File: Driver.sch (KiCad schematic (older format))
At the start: 10 parts

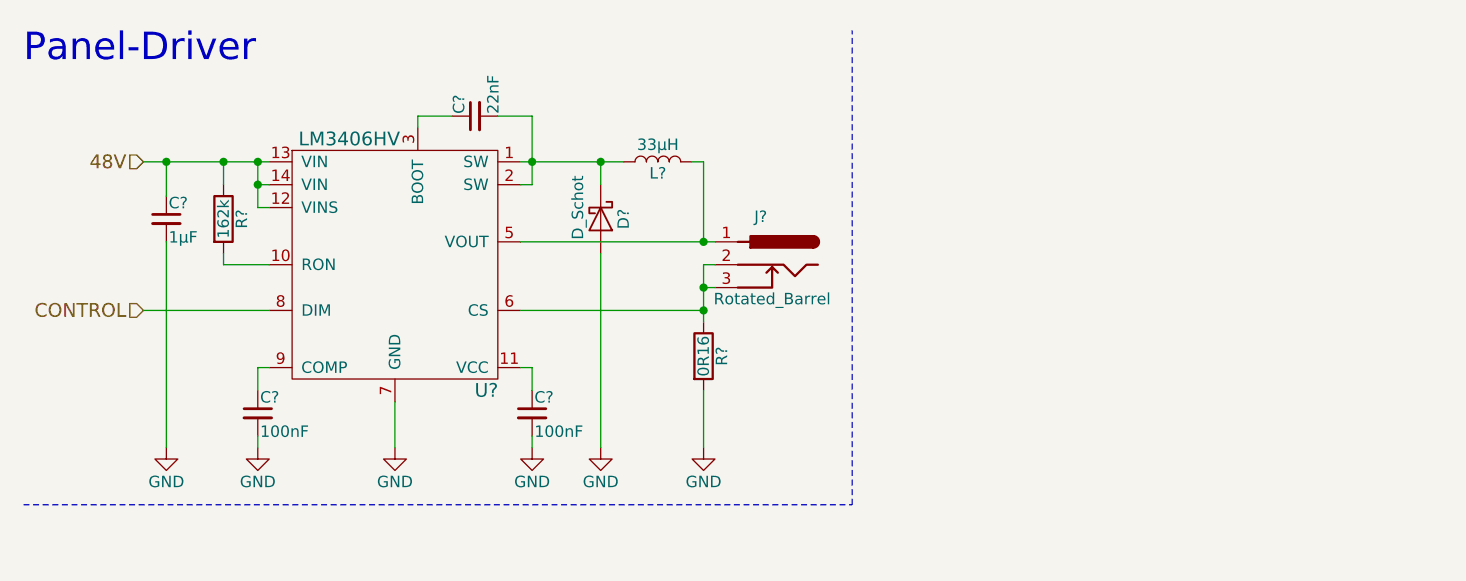
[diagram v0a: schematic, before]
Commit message: Merged RGB- and Panel-Drivers into a single Sheet
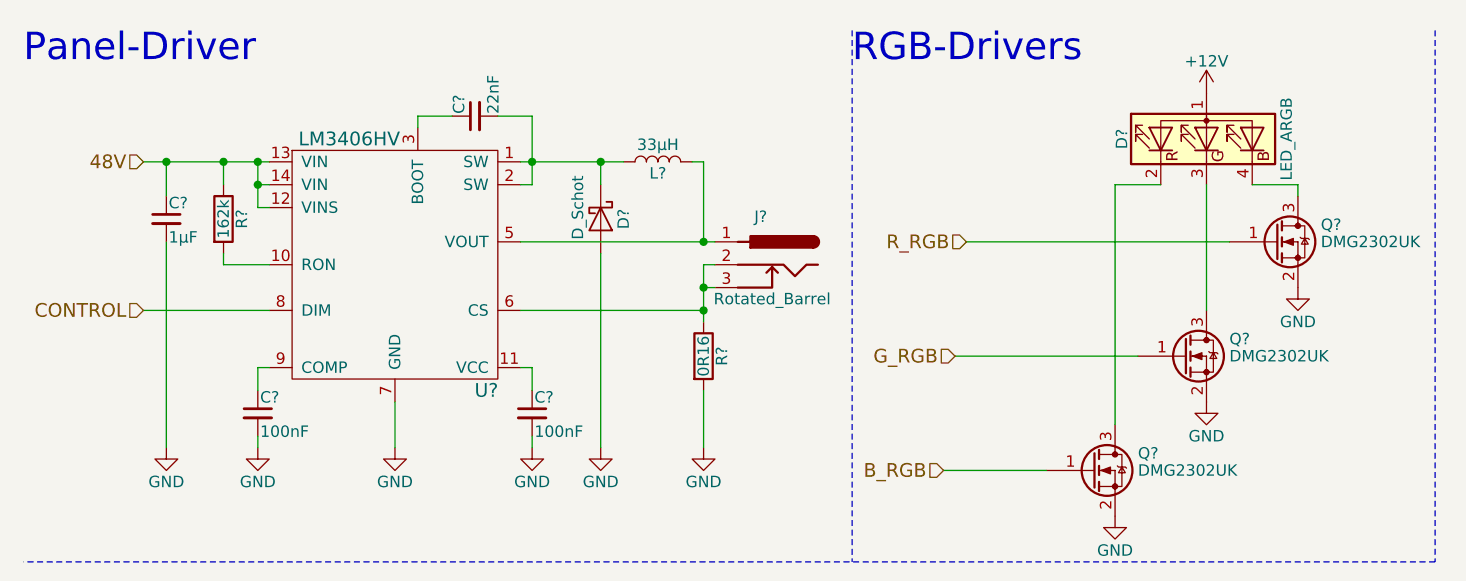
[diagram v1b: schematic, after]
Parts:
- added D?: LED_ARGB, symbol LED_ARGB
- added Q? (x3): DMG2302UK, TO_SOT_Packages_SMD:SOT-23, symbol 2N7002
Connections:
- net GND: now also Q?.2 (S), Q?.2 (S), Q?.2 (S)
- new net: D?.2 (RK), Q?.3 (D)
- new net: D?.3 (GK), Q?.3 (D)
- new net: D?.4 (BK), Q?.3 (D)
- new net +12V: D?.1 (A)
- new net B_RGB: Q?.1 (G)
- new net G_RGB: Q?.1 (G)
- new net R_RGB: Q?.1 (G)
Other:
- note added: "RGB-Drivers"
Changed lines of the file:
@@
 $Descr A4 11693 8268
 encoding utf-8
-Sheet 4 5
+Sheet 3 5
 Title ""
 Date ""
@@
 AR Path="/5A4C3F5F/5A777BDD" Ref="#PWR043"  Part="1"
 AR Path="/5A4C34AF/5A777BDD" Ref="#PWR038"  Part="1"
-F 0 "#PWR043" H 1500 2050 50  0001 C CNN
+F 0 "#PWR038" H 1500 2050 50  0001 C CNN
 F 1 "GND" H 1500 2150 50  0000 C CNN
 F 2 "" H 1500 2300 50  0001 C CNN
@@
 AR Path="/5A4C3F5F/5A777CDA" Ref="#PWR044"  Part="1"
 AR Path="/5A4C34AF/5A777CDA" Ref="#PWR039"  Part="1"
-F 0 "#PWR044" H 2700 2050 50  0001 C CNN
+F 0 "#PWR039" H 2700 2050 50  0001 C CNN
 F 1 "GND" H 2700 2150 50  0000 C CNN
 F 2 "" H 2700 2300 50  0001 C CNN
@@
 AR Path="/5A4C3F5F/5A777FA3" Ref="#PWR045"  Part="1"
 AR Path="/5A4C34AF/5A777FA3" Ref="#PWR040"  Part="1"
-F 0 "#PWR045" H 2100 2050 50  0001 C CNN
+F 0 "#PWR040" H 2100 2050 50  0001 C CNN
 F 1 "GND" H 2100 2150 50  0000 C CNN
 F 2 "" H 2100 2300 50  0001 C CNN
@@
 AR Path="/5A4C3F5F/5A778B62" Ref="#PWR046"  Part="1"
 AR Path="/5A4C34AF/5A778B62" Ref="#PWR041"  Part="1"
-F 0 "#PWR046" H 3000 2050 50  0001 C CNN
+F 0 "#PWR041" H 3000 2050 50  0001 C CNN
 F 1 "GND" H 3000 2150 50  0000 C CNN
 F 2 "" H 3000 2300 50  0001 C CNN
@@
 AR Path="/5A4C34AF/5A77A9CB" Ref="#PWR042"  Part="1"
 AR Path="/5A4C3F5F/5A77A9CB" Ref="#PWR047"  Part="1"
-F 0 "#PWR047" H 3450 2050 50  0001 C CNN
+F 0 "#PWR042" H 3450 2050 50  0001 C CNN
 F 1 "GND" H 3450 2150 50  0000 C CNN
 F 2 "" H 3450 2300 50  0001 C CNN
@@
 Text Notes 475  625  0    120  ~ 0
 Panel-Driver
+Text HLabel 4600 1400 0    60   Input ~ 0
+R_RGB
+Text HLabel 4500 2400 0    60   Input ~ 0
+B_RGB
+Text HLabel 4550 1900 0    60   Input ~ 0
+G_RGB
+$Comp
+L LED_ARGB D?
+U 1 1 5A83A3D8
+P 5650 950
+F 0 "D?" H 5650 1320 50  0000 C CNN
+F 1 "LED_ARGB" H 5650 600 50  0000 C CNN
+F 2 "" H 5650 900 50  0001 C CNN
+F 3 "" H 5650 900 50  0001 C CNN
+	1    5650 950
+	0    -1   -1   0
+$EndComp
+$Comp
+L +12V #PWR?
+U 1 1 5A83A3DF
+P 5650 750
+F 0 "#PWR?" H 5650 600 50  0001 C CNN
+F 1 "+12V" H 5650 890 50  0000 C CNN
+F 2 "" H 5650 750 50  0001 C CNN
+F 3 "" H 5650 750 50  0001 C CNN
+	1    5650 750
+	1    0    0    -1
+$EndComp
+Wire Wire Line
+	5250 1150 5450 1150
+Wire Wire Line
+	4600 1400 5750 1400
+Wire Wire Line
+	4550 1900 5350 1900
+Wire Wire Line
+	4500 2400 4950 2400
+$Comp
+L GND #PWR?
+U 1 1 5A83A3E9
+P 6050 1600
+F 0 "#PWR?" H 6050 1350 50  0001 C CNN
+F 1 "GND" H 6050 1450 50  0000 C CNN
+F 2 "" H 6050 1600 50  0001 C CNN
+F 3 "" H 6050 1600 50  0001 C CNN
+	1    6050 1600
+	1    0    0    -1
+$EndComp
+$Comp
+L GND #PWR?
+U 1 1 5A83A3EF
+P 5650 2100
+F 0 "#PWR?" H 5650 1850 50  0001 C CNN
+F 1 "GND" H 5650 1950 50  0000 C CNN
+F 2 "" H 5650 2100 50  0001 C CNN
+F 3 "" H 5650 2100 50  0001 C CNN
+	1    5650 2100
+	1    0    0    -1
+$EndComp
+$Comp
+L GND #PWR?
+U 1 1 5A83A3F5
+P 5250 2600
+F 0 "#PWR?" H 5250 2350 50  0001 C CNN
+F 1 "GND" H 5250 2450 50  0000 C CNN
+F 2 "" H 5250 2600 50  0001 C CNN
+F 3 "" H 5250 2600 50  0001 C CNN
+	1    5250 2600
+	1    0    0    -1
+$EndComp
+Wire Wire Line
+	5250 1150 5250 2200
+Wire Wire Line
+	5650 1150 5650 1700
+$Comp
+L 2N7002 Q?
+U 1 1 5A83A3FE
+P 5150 2400
+F 0 "Q?" H 5350 2475 50  0000 L CNN
+F 1 "DMG2302UK" H 5350 2400 50  0000 L CNN
+F 2 "TO_SOT_Packages_SMD:SOT-23" H 5350 2325 50  0001 L CIN
+F 3 "https://www.diodes.com/assets/Datasheets/DMG2302UK.pdf" H 5150 2400 50  0001 L CNN
+F 4 "https://www.digikey.com/product-detail/en/diodes-incorporated/DMG2302UK-7/DMG2302UK-7DICT-ND/6010163" H 5150 2400 60  0001 C CNN "Digikey"
+	1    5150 2400
+	1    0    0    -1
+$EndComp
+$Comp
+L 2N7002 Q?
+U 1 1 5A83A406
+P 5550 1900
+F 0 "Q?" H 5750 1975 50  0000 L CNN
+F 1 "DMG2302UK" H 5750 1900 50  0000 L CNN
+F 2 "TO_SOT_Packages_SMD:SOT-23" H 5750 1825 50  0001 L CIN
+F 3 "https://www.diodes.com/assets/Datasheets/DMG2302UK.pdf" H 5550 1900 50  0001 L CNN
+F 4 "https://www.digikey.com/product-detail/en/diodes-incorporated/DMG2302UK-7/DMG2302UK-7DICT-ND/6010163" H 5550 1900 60  0001 C CNN "Digikey"
+	1    5550 1900
+	1    0    0    -1
+$EndComp
+$Comp
+L 2N7002 Q?
+U 1 1 5A83A40E
+P 5950 1400
+F 0 "Q?" H 6150 1475 50  0000 L CNN
+F 1 "DMG2302UK" H 6150 1400 50  0000 L CNN
+F 2 "TO_SOT_Packages_SMD:SOT-23" H 6150 1325 50  0001 L CIN
+F 3 "https://www.diodes.com/assets/Datasheets/DMG2302UK.pdf" H 5950 1400 50  0001 L CNN
+F 4 "https://www.digikey.com/product-detail/en/diodes-incorporated/DMG2302UK-7/DMG2302UK-7DICT-ND/6010163" H 5950 1400 60  0001 C CNN "Digikey"
+	1    5950 1400
+	1    0    0    -1
+$EndComp
+Wire Wire Line
+	6050 1200 6050 1150
+Wire Wire Line
+	6050 1150 5850 1150
+Text Notes 4100 625  0    120  ~ 0
+RGB-Drivers
 Wire Notes Line
-	475  2550 4100 2550
+	6650 2800 475  2800
 Wire Notes Line
-	4100 2550 4100 475
+	6650 475  6650 2800
+Wire Notes Line
+	4100 475  4100 2800
 $EndSCHEMATC

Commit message: Moved the transceivers into their own sheet
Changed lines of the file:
@@
 $Descr A4 11693 8268
 encoding utf-8
-Sheet 3 5
+Sheet 4 7
 Title ""
 Date ""
@@
 AR Path="/5A4C3F5F/5A777BDD" Ref="#PWR043"  Part="1"
 AR Path="/5A4C34AF/5A777BDD" Ref="#PWR038"  Part="1"
-F 0 "#PWR038" H 1500 2050 50  0001 C CNN
+F 0 "#PWR043" H 1500 2050 50  0001 C CNN
 F 1 "GND" H 1500 2150 50  0000 C CNN
 F 2 "" H 1500 2300 50  0001 C CNN
@@
 AR Path="/5A4C3F5F/5A777CDA" Ref="#PWR044"  Part="1"
 AR Path="/5A4C34AF/5A777CDA" Ref="#PWR039"  Part="1"
-F 0 "#PWR039" H 2700 2050 50  0001 C CNN
+F 0 "#PWR044" H 2700 2050 50  0001 C CNN
 F 1 "GND" H 2700 2150 50  0000 C CNN
 F 2 "" H 2700 2300 50  0001 C CNN
@@
 AR Path="/5A4C3F5F/5A777FA3" Ref="#PWR045"  Part="1"
 AR Path="/5A4C34AF/5A777FA3" Ref="#PWR040"  Part="1"
-F 0 "#PWR040" H 2100 2050 50  0001 C CNN
+F 0 "#PWR045" H 2100 2050 50  0001 C CNN
 F 1 "GND" H 2100 2150 50  0000 C CNN
 F 2 "" H 2100 2300 50  0001 C CNN
@@
 	1500 1250 1550 1250
 Wire Wire Line
-	1500 1050 1500 1150
-Wire Wire Line
-	1500 1150 1500 1250
+	1500 1050 1500 1250
 Wire Wire Line
 	1500 1150 1550 1150
 Connection ~ 1500 1150
 Wire Wire Line
-	1000 1050 1100 1050
-Wire Wire Line
-	1100 1050 1350 1050
-Wire Wire Line
-	1350 1050 1500 1050
-Wire Wire Line
-	1500 1050 1550 1050
+	1000 1050 1550 1050
 Connection ~ 1500 1050
 Wire Wire Line
@@
 	2550 850  2700 850
 Wire Wire Line
-	2650 1050 2700 1050
-Wire Wire Line
-	2700 1050 3000 1050
-Wire Wire Line
-	3000 1050 3100 1050
-Wire Wire Line
-	2700 850  2700 1050
-Wire Wire Line
-	2700 1050 2700 1150
+	2650 1050 3100 1050
+Wire Wire Line
+	2700 850  2700 1150
 Wire Wire Line
 	1350 1500 1350 1450
@@
 AR Path="/5A4C3F5F/5A778B62" Ref="#PWR046"  Part="1"
 AR Path="/5A4C34AF/5A778B62" Ref="#PWR041"  Part="1"
-F 0 "#PWR041" H 3000 2050 50  0001 C CNN
+F 0 "#PWR046" H 3000 2050 50  0001 C CNN
 F 1 "GND" H 3000 2150 50  0000 C CNN
 F 2 "" H 3000 2300 50  0001 C CNN
@@
 	3450 1050 3450 1400
 Wire Wire Line
-	2650 1400 3450 1400
-Wire Wire Line
-	3450 1400 3500 1400
+	2650 1400 3500 1400
 Connection ~ 3450 1400
 $Comp
@@
 $EndComp
 Wire Wire Line
-	3450 1500 3450 1600
-Wire Wire Line
-	3450 1600 3450 1700
-Wire Wire Line
-	3450 1700 3450 1750
+	3450 1500 3450 1750
 Wire Wire Line
 	3450 1500 3500 1500
@@
 AR Path="/5A4C34AF/5A77A9CB" Ref="#PWR042"  Part="1"
 AR Path="/5A4C3F5F/5A77A9CB" Ref="#PWR047"  Part="1"
-F 0 "#PWR042" H 3450 2050 50  0001 C CNN
+F 0 "#PWR047" H 3450 2050 50  0001 C CNN
 F 1 "GND" H 3450 2150 50  0000 C CNN
 F 2 "" H 3450 2300 50  0001 C CNN

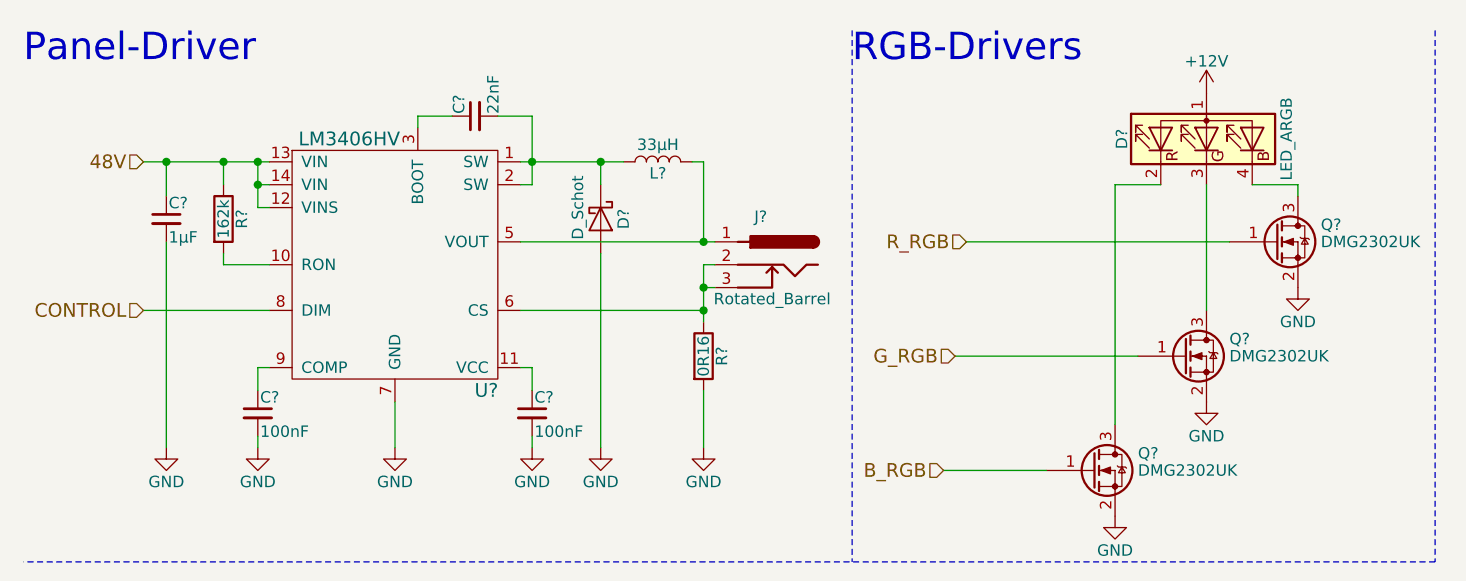
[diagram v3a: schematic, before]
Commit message: Added Gate-Resistors
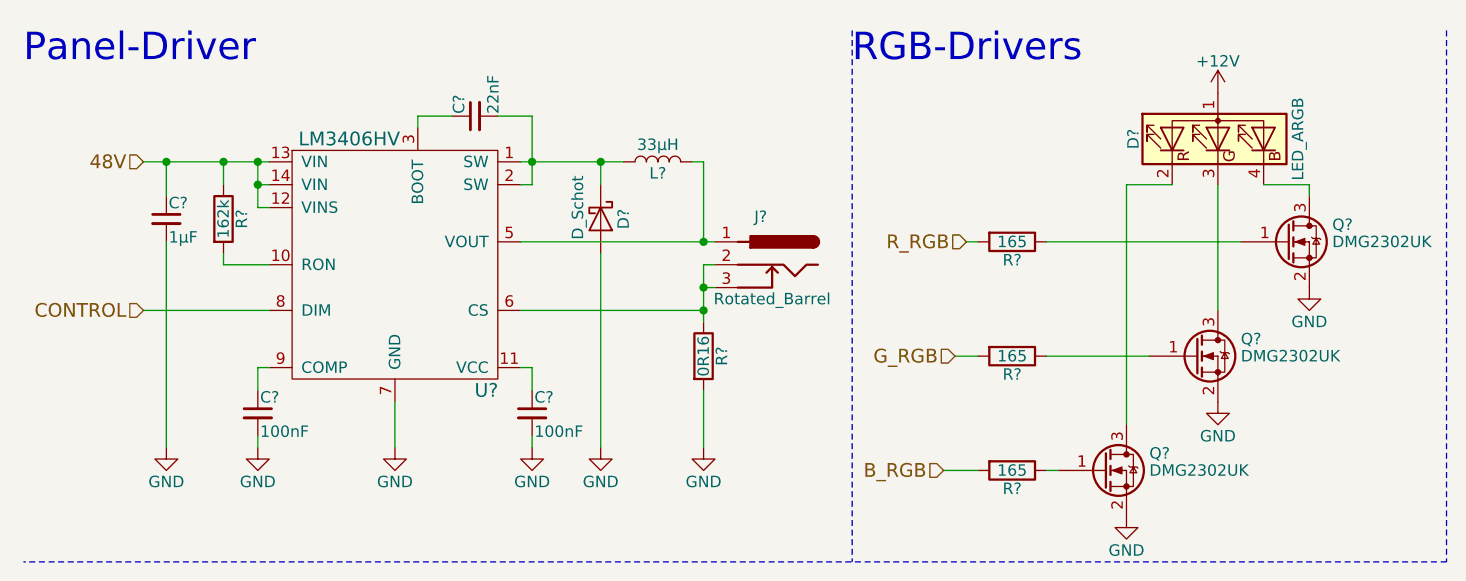
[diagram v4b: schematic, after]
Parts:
- added R? (x3): 165, symbol R
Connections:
- net B_RGB: now also R?.2; no longer Q?.1 (G)
- net G_RGB: now also R?.2; no longer Q?.1 (G)
- net R_RGB: now also R?.2; no longer Q?.1 (G)
- new net: Q?.1 (G), R?.1 (x3)
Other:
- moved on the sheet: D?, Q?
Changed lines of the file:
@@
 L LED_ARGB D?
 U 1 1 5A83A3D8
-P 5650 950
+P 5700 950
 AR Path="/5A4C3F5F/5A83A3D8" Ref="D?"  Part="1"
 AR Path="/5A4C442B/5A83A3D8" Ref="D?"  Part="1"
-F 0 "D?" H 5650 1320 50  0000 C CNN
-F 1 "LED_ARGB" H 5650 600 50  0000 C CNN
-F 2 "" H 5650 900 50  0001 C CNN
-F 3 "" H 5650 900 50  0001 C CNN
-	1    5650 950
+F 0 "D?" H 5700 1320 50  0000 C CNN
+F 1 "LED_ARGB" H 5700 600 50  0000 C CNN
+F 2 "" H 5700 900 50  0001 C CNN
+F 3 "" H 5700 900 50  0001 C CNN
+	1    5700 950
 	0    -1   -1   0
 $EndComp
@@
 L +12V #PWR?
 U 1 1 5A83A3DF
-P 5650 750
+P 5700 750
 AR Path="/5A4C3F5F/5A83A3DF" Ref="#PWR?"  Part="1"
 AR Path="/5A4C442B/5A83A3DF" Ref="#PWR?"  Part="1"
-F 0 "#PWR?" H 5650 600 50  0001 C CNN
-F 1 "+12V" H 5650 890 50  0000 C CNN
-F 2 "" H 5650 750 50  0001 C CNN
-F 3 "" H 5650 750 50  0001 C CNN
-	1    5650 750
+F 0 "#PWR?" H 5700 600 50  0001 C CNN
+F 1 "+12V" H 5700 890 50  0000 C CNN
+F 2 "" H 5700 750 50  0001 C CNN
+F 3 "" H 5700 750 50  0001 C CNN
+	1    5700 750
 	1    0    0    -1
 $EndComp
 Wire Wire Line
-	5250 1150 5450 1150
+	5300 1150 5500 1150
 Wire Wire Line
-	4600 1400 5750 1400
-Wire Wire Line
-	4550 1900 5350 1900
-Wire Wire Line
-	4500 2400 4950 2400
+	4950 1900 5400 1900
 $Comp
 L GND #PWR?
 U 1 1 5A83A3E9
-P 6050 1600
+P 6100 1600
 AR Path="/5A4C3F5F/5A83A3E9" Ref="#PWR?"  Part="1"
 AR Path="/5A4C442B/5A83A3E9" Ref="#PWR?"  Part="1"
-F 0 "#PWR?" H 6050 1350 50  0001 C CNN
-F 1 "GND" H 6050 1450 50  0000 C CNN
-F 2 "" H 6050 1600 50  0001 C CNN
-F 3 "" H 6050 1600 50  0001 C CNN
-	1    6050 1600
+F 0 "#PWR?" H 6100 1350 50  0001 C CNN
+F 1 "GND" H 6100 1450 50  0000 C CNN
+F 2 "" H 6100 1600 50  0001 C CNN
+F 3 "" H 6100 1600 50  0001 C CNN
+	1    6100 1600
 	1    0    0    -1
 $EndComp
@@
 L GND #PWR?
 U 1 1 5A83A3EF
-P 5650 2100
+P 5700 2100
 AR Path="/5A4C3F5F/5A83A3EF" Ref="#PWR?"  Part="1"
 AR Path="/5A4C442B/5A83A3EF" Ref="#PWR?"  Part="1"
-F 0 "#PWR?" H 5650 1850 50  0001 C CNN
-F 1 "GND" H 5650 1950 50  0000 C CNN
-F 2 "" H 5650 2100 50  0001 C CNN
-F 3 "" H 5650 2100 50  0001 C CNN
-	1    5650 2100
+F 0 "#PWR?" H 5700 1850 50  0001 C CNN
+F 1 "GND" H 5700 1950 50  0000 C CNN
+F 2 "" H 5700 2100 50  0001 C CNN
+F 3 "" H 5700 2100 50  0001 C CNN
+	1    5700 2100
 	1    0    0    -1
 $EndComp
@@
 L GND #PWR?
 U 1 1 5A83A3F5
-P 5250 2600
+P 5300 2600
 AR Path="/5A4C3F5F/5A83A3F5" Ref="#PWR?"  Part="1"
 AR Path="/5A4C442B/5A83A3F5" Ref="#PWR?"  Part="1"
-F 0 "#PWR?" H 5250 2350 50  0001 C CNN
-F 1 "GND" H 5250 2450 50  0000 C CNN
-F 2 "" H 5250 2600 50  0001 C CNN
-F 3 "" H 5250 2600 50  0001 C CNN
-	1    5250 2600
+F 0 "#PWR?" H 5300 2350 50  0001 C CNN
+F 1 "GND" H 5300 2450 50  0000 C CNN
+F 2 "" H 5300 2600 50  0001 C CNN
+F 3 "" H 5300 2600 50  0001 C CNN
+	1    5300 2600
 	1    0    0    -1
 $EndComp
 Wire Wire Line
-	5250 1150 5250 2200
+	5300 1150 5300 2200
 Wire Wire Line
-	5650 1150 5650 1700
+	5700 1150 5700 1700
 $Comp
 L 2N7002 Q?
 U 1 1 5A83A3FE
-P 5150 2400
+P 5200 2400
 AR Path="/5A4C3F5F/5A83A3FE" Ref="Q?"  Part="1"
 AR Path="/5A4C442B/5A83A3FE" Ref="Q?"  Part="1"
-F 0 "Q?" H 5350 2475 50  0000 L CNN
-F 1 "DMG2302UK" H 5350 2400 50  0000 L CNN
-F 2 "TO_SOT_Packages_SMD:SOT-23" H 5350 2325 50  0001 L CIN
-F 3 "https://www.diodes.com/assets/Datasheets/DMG2302UK.pdf" H 5150 2400 50  0001 L CNN
-F 4 "https://www.digikey.com/product-detail/en/diodes-incorporated/DMG2302UK-7/DMG2302UK-7DICT-ND/6010163" H 5150 2400 60  0001 C CNN "Digikey"
-	1    5150 2400
+F 0 "Q?" H 5400 2475 50  0000 L CNN
+F 1 "DMG2302UK" H 5400 2400 50  0000 L CNN
+F 2 "TO_SOT_Packages_SMD:SOT-23" H 5400 2325 50  0001 L CIN
+F 3 "https://www.diodes.com/assets/Datasheets/DMG2302UK.pdf" H 5200 2400 50  0001 L CNN
+F 4 "https://www.digikey.com/product-detail/en/diodes-incorporated/DMG2302UK-7/DMG2302UK-7DICT-ND/6010163" H 5200 2400 60  0001 C CNN "Digikey"
+	1    5200 2400
 	1    0    0    -1
 $EndComp
@@
 L 2N7002 Q?
 U 1 1 5A83A406
-P 5550 1900
+P 5600 1900
 AR Path="/5A4C3F5F/5A83A406" Ref="Q?"  Part="1"
 AR Path="/5A4C442B/5A83A406" Ref="Q?"  Part="1"
-F 0 "Q?" H 5750 1975 50  0000 L CNN
-F 1 "DMG2302UK" H 5750 1900 50  0000 L CNN
-F 2 "TO_SOT_Packages_SMD:SOT-23" H 5750 1825 50  0001 L CIN
-F 3 "https://www.diodes.com/assets/Datasheets/DMG2302UK.pdf" H 5550 1900 50  0001 L CNN
-F 4 "https://www.digikey.com/product-detail/en/diodes-incorporated/DMG2302UK-7/DMG2302UK-7DICT-ND/6010163" H 5550 1900 60  0001 C CNN "Digikey"
-	1    5550 1900
+F 0 "Q?" H 5800 1975 50  0000 L CNN
+F 1 "DMG2302UK" H 5800 1900 50  0000 L CNN
+F 2 "TO_SOT_Packages_SMD:SOT-23" H 5800 1825 50  0001 L CIN
+F 3 "https://www.diodes.com/assets/Datasheets/DMG2302UK.pdf" H 5600 1900 50  0001 L CNN
+F 4 "https://www.digikey.com/product-detail/en/diodes-incorporated/DMG2302UK-7/DMG2302UK-7DICT-ND/6010163" H 5600 1900 60  0001 C CNN "Digikey"
+	1    5600 1900
 	1    0    0    -1
 $EndComp
@@
 L 2N7002 Q?
 U 1 1 5A83A40E
-P 5950 1400
+P 6000 1400
 AR Path="/5A4C3F5F/5A83A40E" Ref="Q?"  Part="1"
 AR Path="/5A4C442B/5A83A40E" Ref="Q?"  Part="1"
-F 0 "Q?" H 6150 1475 50  0000 L CNN
-F 1 "DMG2302UK" H 6150 1400 50  0000 L CNN
-F 2 "TO_SOT_Packages_SMD:SOT-23" H 6150 1325 50  0001 L CIN
-F 3 "https://www.diodes.com/assets/Datasheets/DMG2302UK.pdf" H 5950 1400 50  0001 L CNN
-F 4 "https://www.digikey.com/product-detail/en/diodes-incorporated/DMG2302UK-7/DMG2302UK-7DICT-ND/6010163" H 5950 1400 60  0001 C CNN "Digikey"
-	1    5950 1400
+F 0 "Q?" H 6200 1475 50  0000 L CNN
+F 1 "DMG2302UK" H 6200 1400 50  0000 L CNN
+F 2 "TO_SOT_Packages_SMD:SOT-23" H 6200 1325 50  0001 L CIN
+F 3 "https://www.diodes.com/assets/Datasheets/DMG2302UK.pdf" H 6000 1400 50  0001 L CNN
+F 4 "https://www.digikey.com/product-detail/en/diodes-incorporated/DMG2302UK-7/DMG2302UK-7DICT-ND/6010163" H 6000 1400 60  0001 C CNN "Digikey"
+	1    6000 1400
 	1    0    0    -1
 $EndComp
 Wire Wire Line
-	6050 1200 6050 1150
+	6100 1200 6100 1150
 Wire Wire Line
-	6050 1150 5850 1150
+	6100 1150 5900 1150
 Text Notes 4100 625  0    120  ~ 0
 RGB-Drivers
 Wire Notes Line
-	6650 2800 475  2800
+	6700 2800 475  2800
 Wire Notes Line
-	6650 475  6650 2800
+	6700 475  6700 2800
 Wire Notes Line
 	4100 475  4100 2800
+Wire Wire Line
+	4950 2400 5000 2400
+$Comp
+L R R?
+U 1 1 5A8936F2
+P 4800 1400
+F 0 "R?" V 4880 1400 50  0000 C CNN
+F 1 "165" V 4800 1400 50  0000 C CNN
+F 2 "" V 4730 1400 50  0001 C CNN
+F 3 "" H 4800 1400 50  0001 C CNN
+	1    4800 1400
+	0    1    1    0
+$EndComp
+Wire Wire Line
+	4650 1400 4600 1400
+Wire Wire Line
+	4950 1400 5800 1400
+$Comp
+L R R?
+U 1 1 5A8938B9
+P 4800 1900
+F 0 "R?" V 4880 1900 50  0000 C CNN
+F 1 "165" V 4800 1900 50  0000 C CNN
+F 2 "" V 4730 1900 50  0001 C CNN
+F 3 "" H 4800 1900 50  0001 C CNN
+	1    4800 1900
+	0    1    1    0
+$EndComp
+Wire Wire Line
+	4650 1900 4550 1900
+$Comp
+L R R?
+U 1 1 5A8939A3
+P 4800 2400
+F 0 "R?" V 4880 2400 50  0000 C CNN
+F 1 "165" V 4800 2400 50  0000 C CNN
+F 2 "" V 4730 2400 50  0001 C CNN
+F 3 "" H 4800 2400 50  0001 C CNN
+	1    4800 2400
+	0    1    1    0
+$EndComp
+Wire Wire Line
+	4650 2400 4500 2400
 $EndSCHEMATC
